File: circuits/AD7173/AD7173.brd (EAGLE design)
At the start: 21.4 x 43.9 mm, 32 parts, among them IC1 AD7173, IC2 ADP1720, IC3 ADP1720ARMZ-5, IC4 OPA2134D, IC6 OPA2725DGK

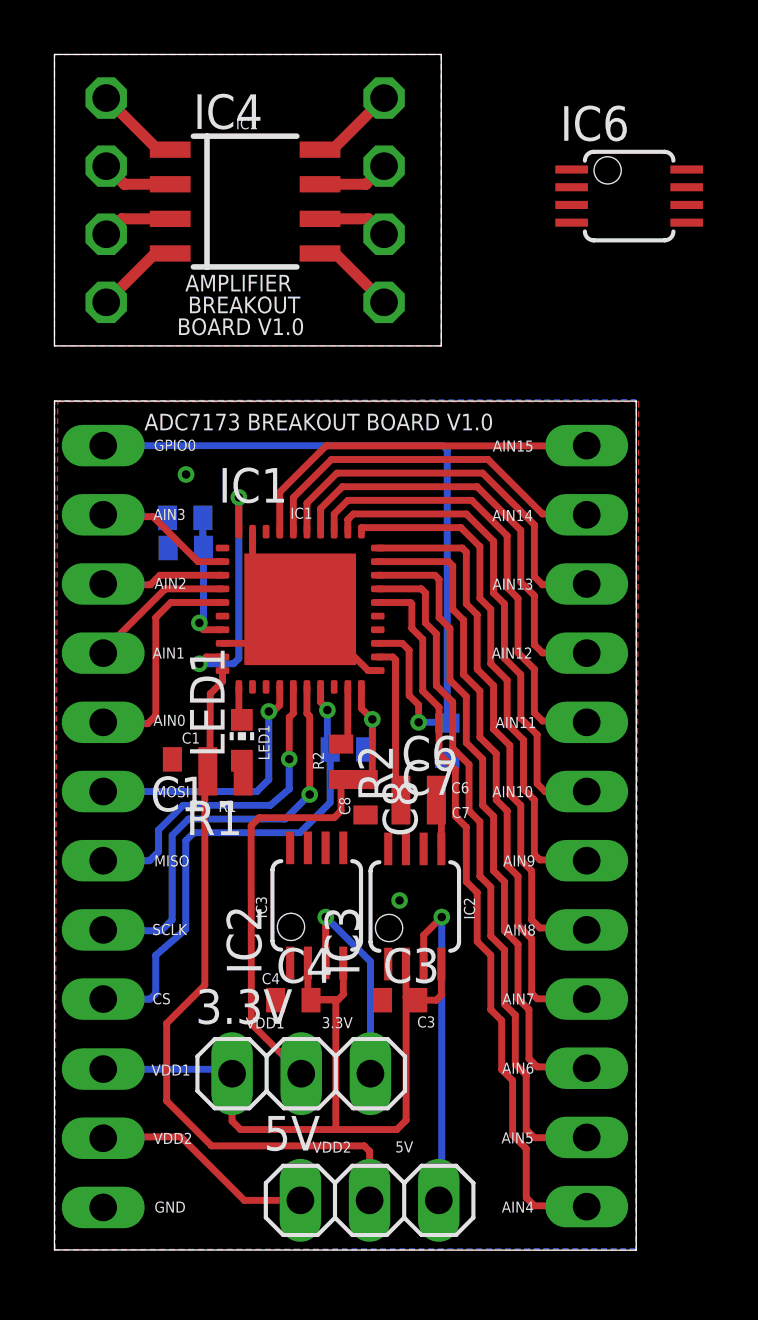
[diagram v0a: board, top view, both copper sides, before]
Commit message: upadted AD7173 circuits
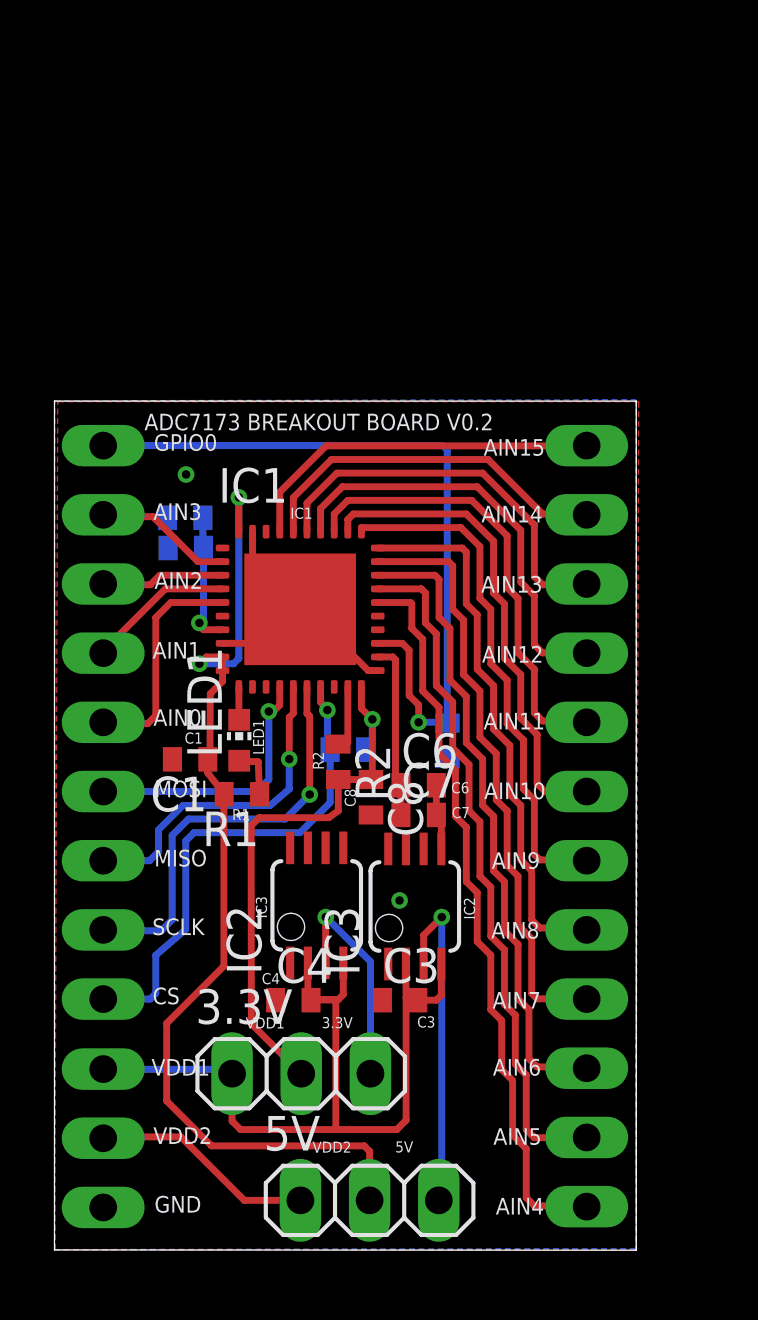
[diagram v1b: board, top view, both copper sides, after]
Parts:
- removed IC4: OPA2134D, linear:SOIC8
- removed IC6: OPA2725DGK, linear:MSOP08
- removed JP1, JP2, JP3, JP4, JP5, JP6, JP7, JP8: (no value), pinhead:1X01
- R1: value 10k -> 220
- moved R1 0.72 mm to (6.88, 16.7)
- moved C8 0.20 mm to (11.6, 16.6)
- moved C6 0.10 mm to (13.4, 17.1)
- moved LED1 0.10 mm to (6.78, 18.7)
- moved R2 0.10 mm to (10.4, 17.9)
- moved C7 0.10 mm to (13.4, 16.0)
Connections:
- removed net N$31: IC4.1, JP1.1
- removed net N$33: IC4.2, JP2.1
- removed net N$34: IC4.3, JP3.1
- removed net N$35: IC4.4, JP4.1
- removed net N$36: IC4.5, JP5.1
- removed net N$37: IC4.6, JP6.1
- removed net N$40: IC4.7, JP7.1
- removed net N$41: IC4.8, JP8.1
- removed net V+: IC6.8
- removed net V-: IC6.4
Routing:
- net N$41: track 3.13 -> 0.00 mm
- net N$31: track 3.13 -> 0.00 mm
- net N$35: track 3.09 -> 0.00 mm
- net N$36: track 3.09 -> 0.00 mm
- net N$40: track 2.63 -> 0.00 mm
- net N$33: track 2.63 -> 0.00 mm
- net N$37: track 2.58 -> 0.00 mm
- net N$34: track 2.58 -> 0.00 mm
- net N$1: track 1.06 -> 1.89 mm
- removed copper zone on layer 1, net N$42
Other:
- board size 21.4 x 43.9 mm -> 21.4 x 31.2 mm
- board text added: "ADC7173 BREAKOUT BOARD V0.2"
- board text removed: "ADC7173 BREAKOUT BOARD V1.0"
- board text removed: "AMPLIFIER"
- board text removed: "BOARD V1.0"
- board text removed: "BREAKOUT"

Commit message: updated AD7173 circuit
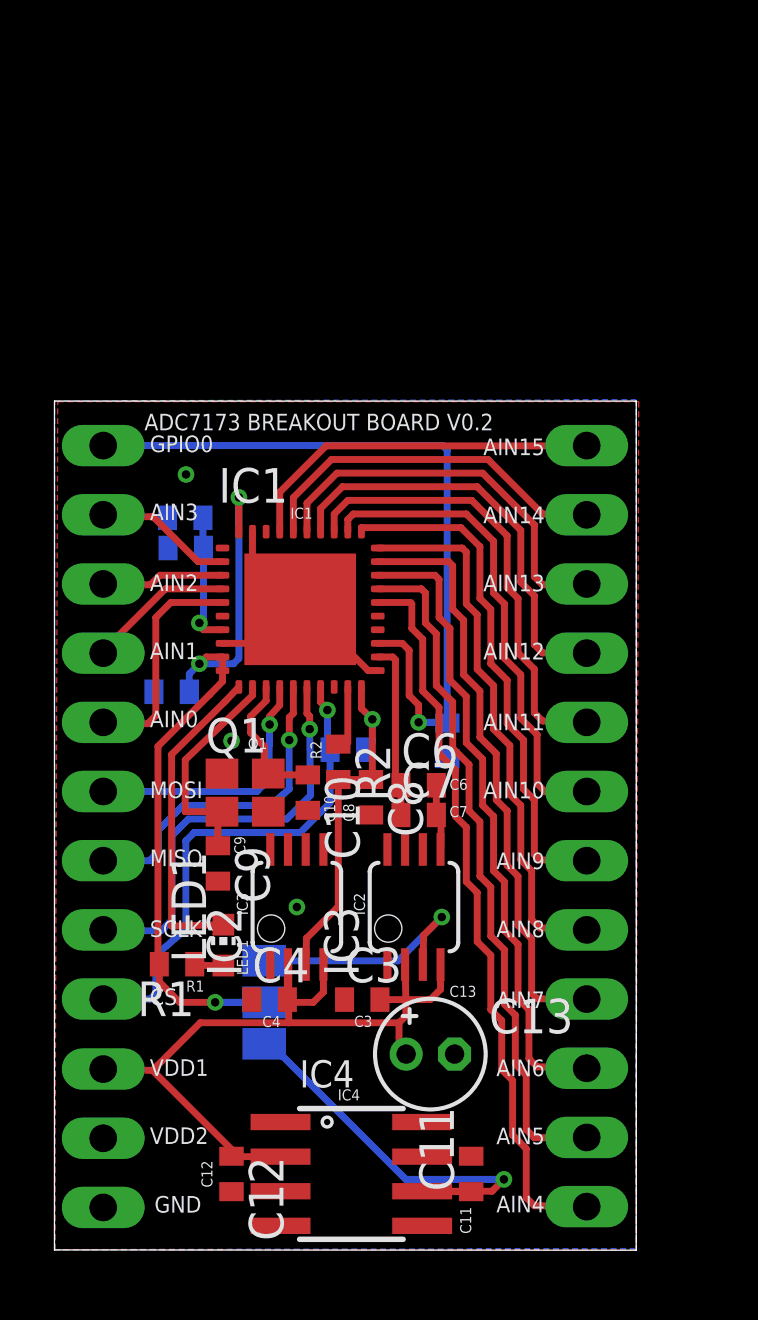
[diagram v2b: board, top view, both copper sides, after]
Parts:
- removed 3.3V, 5V: (no value), pinhead:1X03
- added C10, C11, C12, C9: 0.1uF, rcl:C0402
- added C13: 10uF, rcl:E1,8-4
- added IC4: ADR441AR, kblom:SO8
- added Q1: FA-20H, crystal:FA-20H
- added SJ1: (no value), jumper:SJ_2
- moved LED1 7.54 mm to (6.20, 11.2)
- moved R1 6.68 mm to (4.50, 10.5)
- moved C1 2.57 mm to (4.30, 20.5), flipped to the bottom, turned to 0 degrees
- moved C3 1.39 mm to (11.3, 9.20)
- moved C4 0.87 mm to (7.90, 9.20)
- moved IC2 0.73 mm to (8.90, 12.6)
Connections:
- removed net N$30: 5V.3, IC3.3
- new net V+: C1.1, IC1.10, IC1.40, IC1.9, R1.2, SJ1.2
- new net VIN: C12.1, C13.+, C3.2, C4.2, IC2.2, IC2.4, IC3.2, IC3.4, IC4.2, POWER.1
- net +3V3: now also IC2.3; no longer 3.3V.2
- net +5V: now also IC3.3, SJ1.3; no longer 5V.2, C1.1, IC1.10, IC1.40, IC1.9, R1.2
- net GND: now also C10.2, C11.2, C12.2, C13.-, C9.2, IC4.4, Q1.2, Q1.4
- net N$22: now also C10.1, IC1.13, Q1.3; no longer 5V.1, POWER.2
- net N$27: now also C9.1, IC1.12, Q1.1; no longer 3.3V.3, IC2.3
- net N$28: now also C11.1, IC4.6, SJ1.1; no longer 3.3V.1, C3.2, C4.2, IC2.2, IC2.4, IC3.2, IC3.4, POWER.1
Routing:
- net VIN: track 0.00 -> 30.5 mm
- net +5V: track 37.5 -> 9.20 mm, vias 2 -> 1
- net V+: track 0.00 -> 27.9 mm, vias 0 -> 3
- net N$28: track 31.1 -> 16.1 mm, vias 0 -> 1
- net N$30: track 12.4 -> 0.00 mm, vias 1 -> 0
- net SPI: track 1.21 -> 11.7 mm
- net +3V3: track 20.4 -> 13.3 mm
- net N$22: track 8.26 -> 5.15 mm
- net N$1: track 1.89 -> 1.05 mm
- net N$27: track 8.12 -> 8.44 mm, vias 1 -> 0
- net GND: vias 2 -> 3
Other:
- board text added: "C10"
- board text added: "C11"
- board text added: "C12"
- board text added: "C13"
- board text added: "C9"
- board text added: "IC4"
- board text added: "Q1"
- board text added: "SJ1"
- board text removed: "3.3V"
- board text removed: "5V"

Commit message: updated AD7173 breakout board
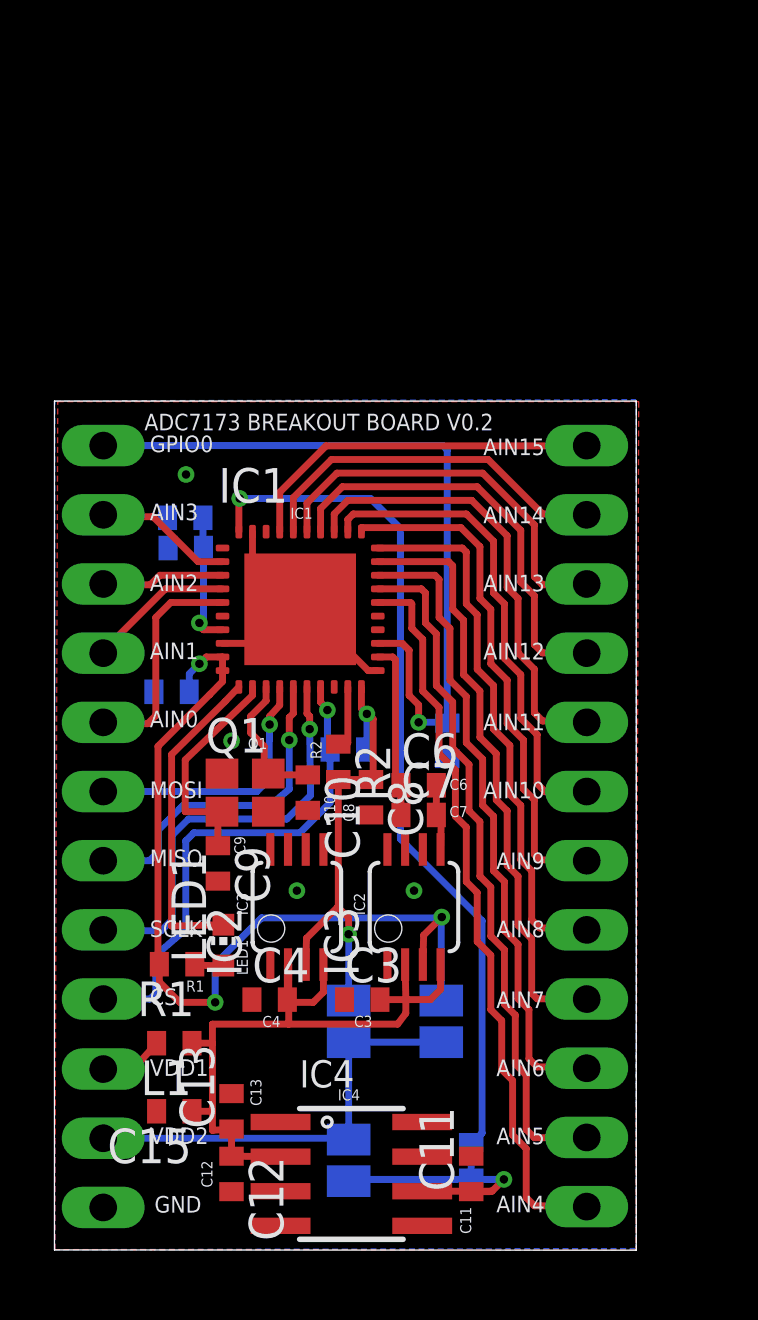
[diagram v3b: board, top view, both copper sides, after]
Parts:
- added C14: 4.7uF, rcl:C0402
- added C15: 0.1uF, rcl:C0402
- added L1: BLM15HB121SN1, inductors:0402
- added SJ2, SJ3: (no value), jumper:SJ
- C10, C9: value 0.1uF -> 10pF
- C13: value 10uF -> 4.7uF; device rcl:E1,8-4 -> rcl:C0402
- C3, C4: value 0.1uF -> 4.7uF
- C5, C7: value 0.1uF -> 1uF
- IC4: value ADR441AR -> ADR445BR
- SJ1: device jumper:SJ_2 -> jumper:SJ
- moved C13 7.60 mm to (6.50, 5.10), turned to 90 degrees
- moved SJ1 6.54 mm to (14.2, 8.40), turned to 270 degrees
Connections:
- removed net V+: C1.1, IC1.10, IC1.40, IC1.9, R1.2, SJ1.2
- new net N$30: L1.2, POWER.1
- new net VCC: C11.1, C14.1, IC1.40, IC4.6, SJ3.1
- net +3V3: now also SJ2.1
- net +5V: now also C1.1, IC1.10, IC1.9, R1.2, SJ1.1; no longer SJ1.3
- net GND: now also C13.2, C14.2, C15.2; no longer C13.-
- net N$28: now also POWER.2, SJ1.2, SJ2.2, SJ3.2; no longer C11.1, IC4.6, SJ1.1
- net VIN: now also C13.1, C15.1, L1.1; no longer C13.+, POWER.1
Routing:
- net VCC: track 0.00 -> 42.6 mm, vias 0 -> 2
- net V+: track 27.9 -> 0.00 mm, vias 3 -> 0
- net +5V: track 9.20 -> 33.0 mm, vias 1 -> 3
- net +3V3: track 13.3 -> 17.0 mm, vias 1 -> 2
- net VIN: track 30.5 -> 27.3 mm
- net N$30: track 0.00 -> 2.38 mm
- net N$28: track 16.1 -> 16.0 mm, vias 1 -> 0
- net GND: vias 3 -> 4
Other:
- board text added: "C14"

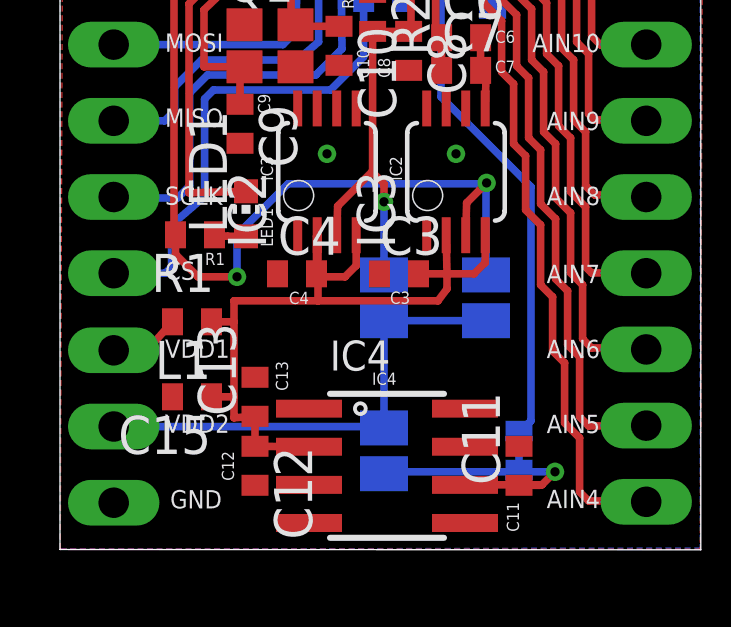
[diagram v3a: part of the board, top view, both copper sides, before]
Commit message: updated AD7173 breakout board
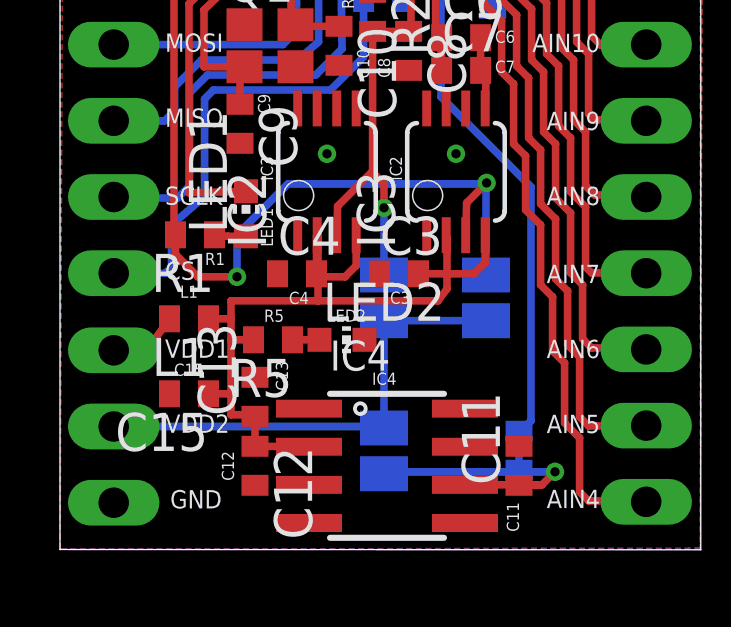
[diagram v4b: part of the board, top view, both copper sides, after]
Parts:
- added LED2: (no value), led:CHIP-LED0603
- added R5: 220, rcl:R0402
- moved C15 0.14 mm to (4.30, 5.20)
- moved L1 0.14 mm to (4.30, 7.70)
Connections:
- new net N$31: LED2.A, R5.1
- net GND: now also LED2.C
- net VIN: now also R5.2
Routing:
- net VIN: track 27.3 -> 28.2 mm
- net N$31: track 0.00 -> 0.90 mm
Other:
- board text added: "AVDD"
- board text added: "C15"
- board text added: "IOVDD"
- board text added: "L1"
- board text added: "LED2"
- board text added: "R5"
- board text added: "REFV"
- board text added: "SJ2"
- board text added: "SJ3"
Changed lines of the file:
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@@
 <text x="5.8" y="2.3" size="0.4064" layer="121" font="vector" ratio="10" rot="R90">C12</text>
 <text x="15.3" y="0.6" size="0.4064" layer="121" font="vector" ratio="10" rot="R90">C11</text>
-<text x="9.2" y="8.2" size="0.4064" layer="122" font="vector" ratio="10" rot="MR270">SJ1</text>
+<text x="15.8" y="9" size="0.4064" layer="122" font="vector" ratio="10" rot="MR270">SJ1</text>
 <text x="16.4" y="4.2" size="0.4064" layer="122" font="vector" ratio="10" rot="MR270">C14</text>
+<text x="8.9" y="7.6" size="0.4064" layer="121" font="vector" ratio="10">LED2</text>
+<text x="6.8" y="7.6" size="0.4064" layer="121" font="vector" ratio="10">R5</text>
+<text x="4" y="8.4" size="0.4064" layer="121" font="vector" ratio="10">L1</text>
+<text x="3.8" y="5.8" size="0.4064" layer="121" font="vector" ratio="10">C15</text>
+<text x="12.4" y="9" size="0.4064" layer="122" font="vector" ratio="10" rot="MR270">SJ2</text>
+<text x="9.5" y="10.9" size="0.6096" layer="122" font="vector" ratio="10" rot="MR180">IOVDD</text>
+<text x="9.7" y="5.9" size="0.6096" layer="122" font="vector" ratio="10" rot="MR180">REFV</text>
+<text x="13" y="10.9" size="0.6096" layer="122" font="vector" ratio="10" rot="MR180">AVDD</text>
+<text x="12.4" y="3.9" size="0.4064" layer="122" font="vector" ratio="10" rot="MR270">SJ3</text>
 </plain>
 <attributes>
@@
 <element name="C13" library="rcl" package="C0402" value="4.7uF" x="6.5" y="5.1" rot="R90"/>
 <element name="C14" library="rcl" package="C0402" value="4.7uF" x="15.3" y="3.3" rot="MR90"/>
-<element name="L1" library="inductors" package="0402" value="BLM15HB121SN1" x="4.4" y="7.6" rot="R180"/>
-<element name="C15" library="rcl" package="C0402" value="0.1uF" x="4.4" y="5.1" rot="R180"/>
+<element name="L1" library="inductors" package="0402" value="BLM15HB121SN1" x="4.3" y="7.7" rot="R180"/>
+<element name="C15" library="rcl" package="C0402" value="0.1uF" x="4.3" y="5.2" rot="R180"/>
 <element name="SJ1" library="jumper" package="SJ" value="" x="14.2" y="8.4" rot="MR270"/>
 <element name="SJ2" library="jumper" package="SJ" value="" x="10.8" y="8.4" rot="MR270"/>
 <element name="SJ3" library="jumper" package="SJ" value="" x="10.8" y="3.3" rot="MR90"/>
+<element name="LED2" library="led" package="CHIP-LED0603" value="" x="9.4" y="7" rot="R270"/>
+<element name="R5" library="rcl" package="R0402" value="220" x="7.1" y="7" rot="R180"/>
 </elements>
 <signals>
@@
 <contactref element="C15" pad="2"/>
 <via x="13.2" y="13.2" extent="1-16" drill="0.31"/>
+<contactref element="LED2" pad="C"/>
 <wire x1="15.3" y1="3.45" x2="15.3" y2="3.95" width="0" layer="19" extent="1-16"/>
 </signal>
@@
 <wire x1="10.42" y1="17.28" x2="10.42" y2="12.62" width="0.254" layer="1"/>
 <contactref element="SJ2" pad="1"/>
-<wire x1="10.8" y1="9.162" x2="10.8" y2="11.6" width="0.254" layer="16"/>
-<via x="10.8" y="11.6" extent="1-16" drill="0.31"/>
-<wire x1="10.8" y1="11.6" x2="10.8" y2="12.2" width="0.254" layer="1"/>
+<wire x1="10.8" y1="9.162" x2="10.8" y2="11.4" width="0.254" layer="16"/>
+<via x="10.8" y="11.4" extent="1-16" drill="0.31"/>
+<wire x1="10.8" y1="11.4" x2="10.8" y2="12.2" width="0.254" layer="1"/>
 <wire x1="10.8" y1="12.2" x2="10.4" y2="12.6" width="0.254" layer="1"/>
 </signal>
@@
 <contactref element="IC2" pad="2"/>
 <contactref element="IC2" pad="4"/>
-<wire x1="5.8" y1="8.3" x2="8.6" y2="8.3" width="0.254" layer="1"/>
+<wire x1="5.7" y1="8.3" x2="8.6" y2="8.3" width="0.254" layer="1"/>
 <wire x1="8.6" y1="8.3" x2="12.6" y2="8.3" width="0.254" layer="1"/>
 <wire x1="12.6" y1="8.3" x2="12.9" y2="8.7" width="0.254" layer="1"/>
 <wire x1="12.9" y1="8.7" x2="12.9" y2="9.2" width="0.254" layer="1"/>
-<wire x1="12.9" y1="9.2" x2="12.874" y2="10.487" width="0.254" layer="1"/>
+<wire x1="12.9" y1="9.2" x2="12.9" y2="10.4" width="0.254" layer="1"/>
+<wire x1="12.9" y1="10.4" x2="12.874" y2="10.487" width="0.254" layer="1"/>
 <wire x1="8.55" y1="9.2" x2="8.55" y2="10.463" width="0.254" layer="1"/>
 <wire x1="8.55" y1="10.463" x2="8.574" y2="10.487" width="0.254" layer="1"/>
@@
 <wire x1="8.3" y1="3.435" x2="6.5" y2="3.45" width="0.254" layer="1"/>
 <contactref element="C13" pad="1"/>
-<wire x1="6.5" y1="4.45" x2="5.8" y2="4.4" width="0.254" layer="1"/>
-<wire x1="5.8" y1="4.4" x2="5.8" y2="5.1" width="0.254" layer="1"/>
-<wire x1="5.8" y1="5.1" x2="5.8" y2="7.6" width="0.254" layer="1"/>
-<wire x1="5.8" y1="7.6" x2="5.8" y2="8.3" width="0.254" layer="1"/>
+<wire x1="6.5" y1="4.45" x2="6.5" y2="4.5" width="0.254" layer="1"/>
+<wire x1="6.5" y1="4.5" x2="5.7" y2="4.5" width="0.254" layer="1"/>
+<wire x1="5.7" y1="4.5" x2="5.7" y2="5.2" width="0.254" layer="1"/>
+<wire x1="5.7" y1="5.2" x2="5.7" y2="7" width="0.254" layer="1"/>
+<wire x1="5.7" y1="7.7" x2="5.7" y2="8.3" width="0.254" layer="1"/>
 <wire x1="6.5" y1="4.45" x2="6.5" y2="3.45" width="0.254" layer="1"/>
 <contactref element="L1" pad="1"/>
 <contactref element="C15" pad="1"/>
-<wire x1="5.05" y1="5.1" x2="5.8" y2="5.1" width="0.254" layer="1"/>
-<wire x1="5.05" y1="7.6" x2="5.8" y2="7.6" width="0.254" layer="1"/>
+<wire x1="4.95" y1="5.2" x2="5.7" y2="5.2" width="0.254" layer="1"/>
+<wire x1="4.95" y1="7.7" x2="5.7" y2="7.7" width="0.254" layer="1"/>
+<contactref element="R5" pad="2"/>
+<wire x1="5.7" y1="7.7" x2="5.7" y2="7" width="0.254" layer="1"/>
+<wire x1="5.7" y1="7" x2="6.45" y2="7" width="0.254" layer="1"/>
 </signal>
 <signal name="VCC">
@@
 <contactref element="L1" pad="2"/>
 <wire x1="1.79" y1="6.65" x2="2.9" y2="6.65" width="0.254" layer="1"/>
-<wire x1="2.9" y1="6.65" x2="3.75" y2="7.6" width="0.254" layer="1"/>
+<wire x1="2.9" y1="6.65" x2="3.65" y2="7.7" width="0.254" layer="1"/>
 </signal>
 <signal name="N$28">
@@
 <wire x1="10.8" y1="7.638" x2="14.2" y2="7.638" width="0.254" layer="16"/>
 </signal>
+<signal name="N$31">
+<contactref element="LED2" pad="A"/>
+<contactref element="R5" pad="1"/>
+<wire x1="7.75" y1="7" x2="8.65" y2="7" width="0.254" layer="1"/>
+</signal>
 </signals>

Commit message: upadted AD7173 breakout board
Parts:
- moved L1 3.61 mm to (7.90, 7.90)
- moved LED2 1.43 mm to (10.8, 6.70)
- moved R5 1.14 mm to (8.20, 6.70)
- moved C13 1.10 mm to (6.40, 6.20)
- moved R4 0.20 mm to (10.8, 18.2)
- moved C6 0.10 mm to (13.4, 17.0)
- moved C12 0.10 mm to (6.40, 2.80)
- moved C3 0.10 mm to (11.3, 9.10)
- moved C4 0.10 mm to (7.90, 9.10)
- moved C7 0.10 mm to (13.4, 15.9)
- moved C8 0.10 mm to (11.5, 16.6)
- moved IC3 0.10 mm to (13.2, 12.5)
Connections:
- net N$30: now also R5.2
- net VIN: no longer R5.2
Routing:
- net VIN: track 28.2 -> 34.1 mm
- net N$30: track 2.40 -> 7.29 mm
- net GND: track 13.5 -> 14.4 mm, vias 4 -> 6
